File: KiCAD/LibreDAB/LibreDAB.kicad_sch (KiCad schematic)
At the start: 0 parts

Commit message: Added a LV bridge prototype module schematic
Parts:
- added C112: 47uF, Capacitor_SMD:C_Elec_10x10.2, symbol Device:C_Polarized
- added C701: 1nF, Capacitor_SMD:C_0805_2012Metric, symbol Device:C
- added J1, J2, J5: 1x3, 1Footprints:PinHeader_1x03_P2.54mm_Vertical, symbol 1Connectors:PinHeader_1x3_2.54mm
- added J3, J4: Conn_01x02_Socket, symbol Connector:Conn_01x02_Socket
- added LOGO1: N/A, 1Footprints:FFE_Logo_12x12mm_Silk, symbol !Mechanical:FFE_logo
- added Q1, Q2, Q3, Q4: SP010N01BGHTO, 1Footprints:TOLL-8-2_ThermalVias, symbol 1Actives:SP010N01BGHTO
- added R1: 1M, Resistor_SMD:R_0805_2012Metric, symbol Device:R_Small
- added R2: 25.6K, Resistor_SMD:R_0805_2012Metric, symbol Device:R_Small
- added R3: 5mR, Resistor_SMD:R_2512_6332Metric, symbol Device:R_Small
- added TP1, TP2, TP3, TP4, TP5, TP6, TP7, TP8: TestPoint_Probe, Footprints:TestPoint_Pad_D1.0mm, symbol Connector:TestPoint_Probe
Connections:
- new net: J1.2 (Pin_2), J4.2 (Pin_2), Q1.2 (S), Q2.3 (D), TP6.1
- new net: J1.1 (Pin_1), Q1.1 (G), TP7.1
- new net: J1.3 (Pin_3), Q2.1 (G), TP8.1
- new net: C112.1, J3.1 (Pin_1), Q1.3 (D), Q3.3 (D), R1.1, TP2.1
- new net: C701.1, J5.1 (Pin_1), R1.2, R2.1, TP3.1
- new net: C112.2, C701.2, J3.2 (Pin_2), J5.2 (Pin_2), R2.2, R3.2, TP1.1
- new net: J5.3 (Pin_3), Q2.2 (S), Q4.2 (S), R3.1, TP4.1
- new net: J2.3 (Pin_3), Q4.1 (G)
- new net: J2.2 (Pin_2), J4.1 (Pin_1), Q3.2 (S), Q4.3 (D), TP5.1
- new net: J2.1 (Pin_1), Q3.1 (G)
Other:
- note added: "Gate driver pins"
- note added: "Screw Terminals"
- note added: "Voltage and Current sense passives"

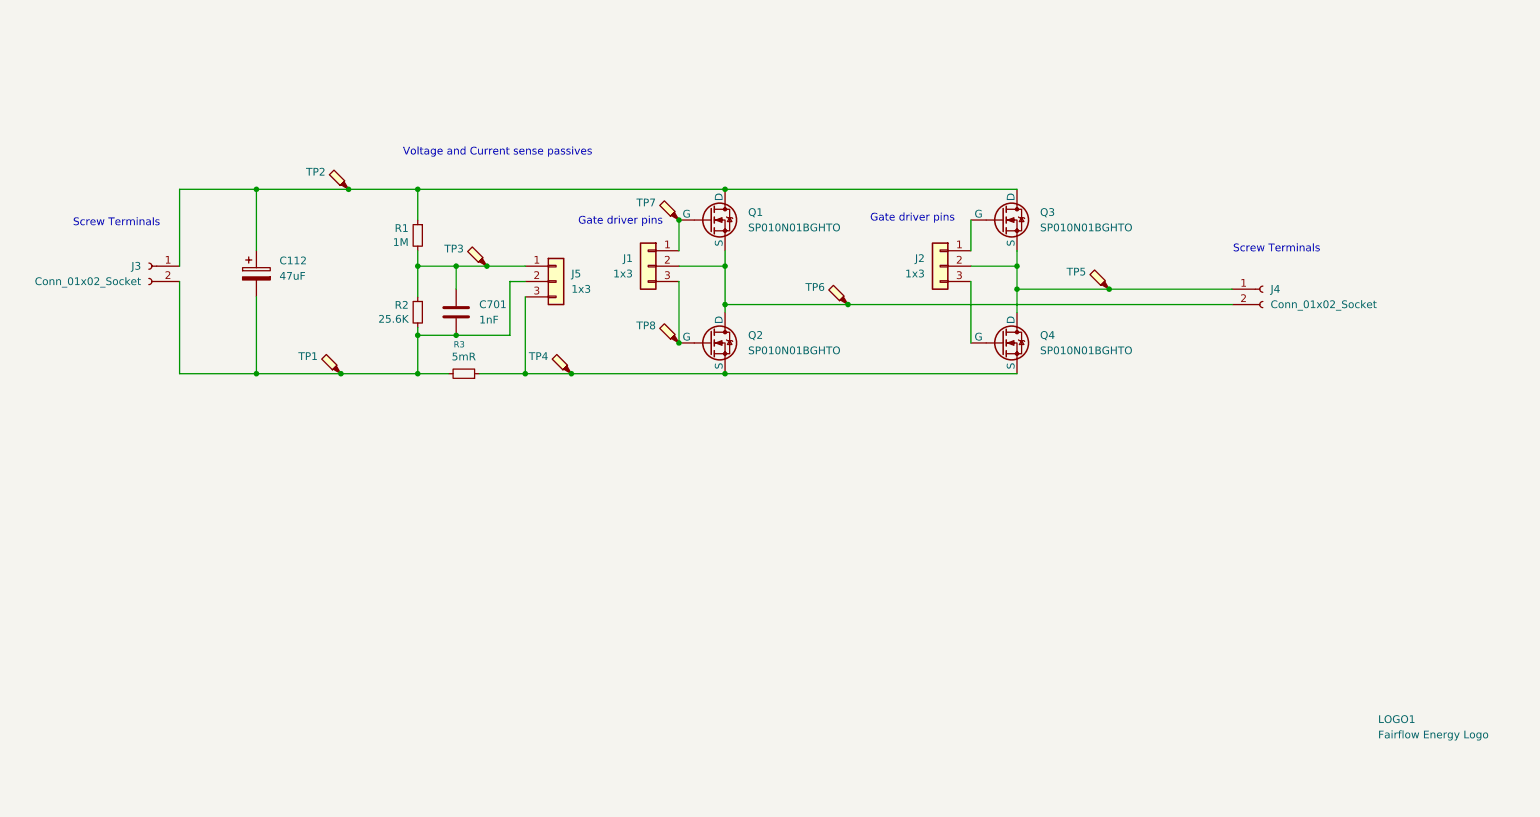
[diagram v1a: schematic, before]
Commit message: Added most footprints from LCSC import
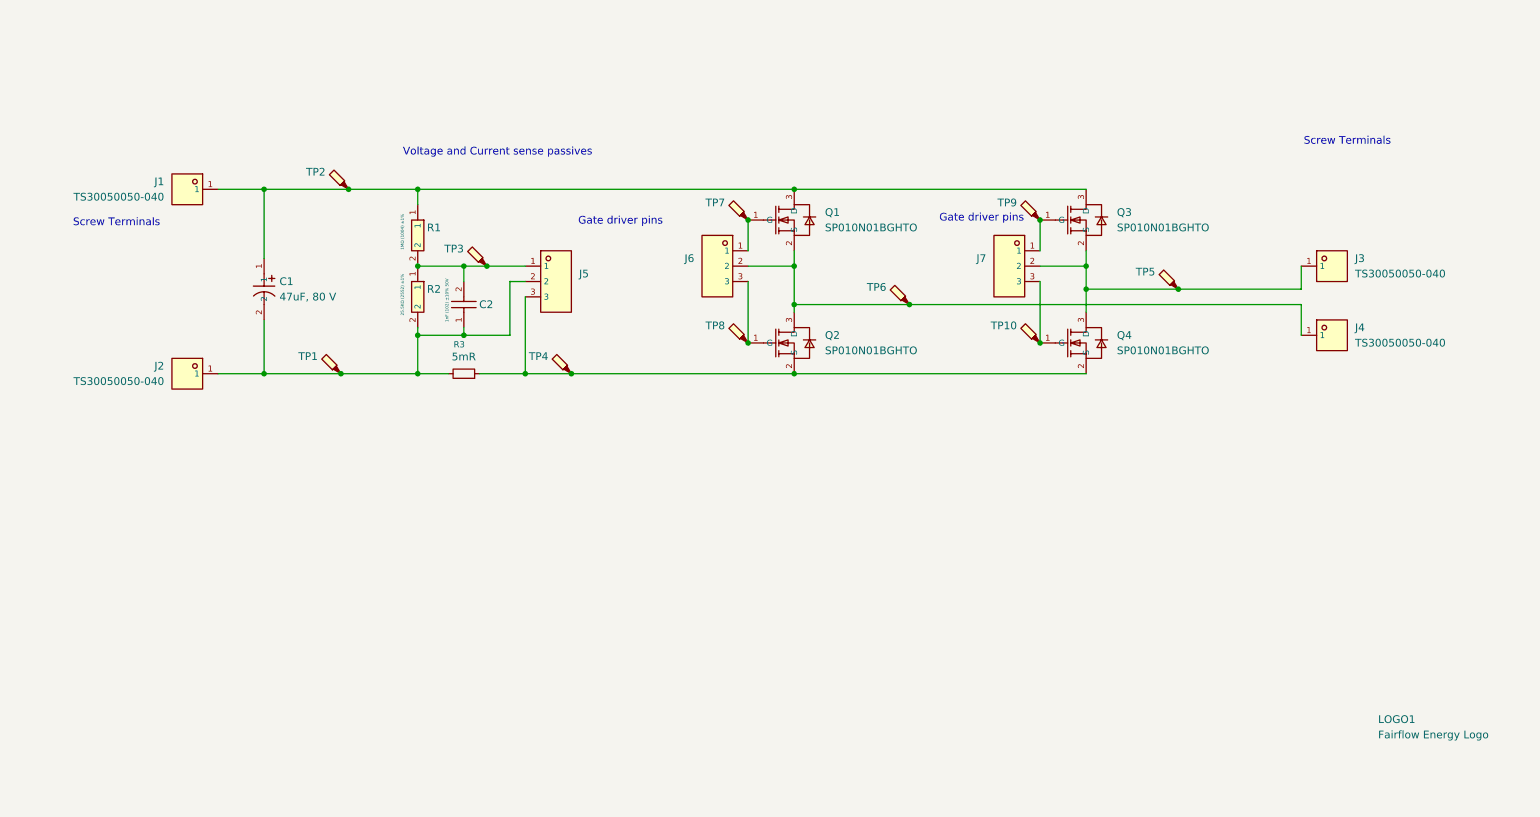
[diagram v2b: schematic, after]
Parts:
- removed C112: 47uF, Capacitor_SMD:C_Elec_10x10.2, symbol Device:C_Polarized
- removed C701: 1nF, Capacitor_SMD:C_0805_2012Metric, symbol Device:C
- removed J1, J2, J5: 1x3, 1Footprints:PinHeader_1x03_P2.54mm_Vertical, symbol 1Connectors:PinHeader_1x3_2.54mm
- removed J3, J4: Conn_01x02_Socket, symbol Connector:Conn_01x02_Socket
- removed Q1, Q2, Q3, Q4: SP010N01BGHTO, 1Footprints:TOLL-8-2_ThermalVias, symbol 1Actives:SP010N01BGHTO
- removed R1: 1M, Resistor_SMD:R_0805_2012Metric, symbol Device:R_Small
- removed R2: 25.6K, Resistor_SMD:R_0805_2012Metric, symbol Device:R_Small
- added C1: 47uF, 80 V, lcsc_footprints:C3031594_CAP-SMD_BD10_0-L10_3-W10_3-FD, symbol lcsc_imported:HBV470M1KTR-1010
- added C2: 1nF (102) ±10% 50V, lcsc_footprints:C46653_C0805, symbol lcsc_imported:1nF_(102)_±10%_50V
- added J1, J2, J3, J4: TS30050050-040, lcsc_footprints:C51018168_SMD_L5_0-W5_0_CON1_5X5_SMD, symbol lcsc_imported:TS30050050-040
- added J5, J6, J7: PZ254VS-11-03P-B01, lcsc_footprints:C41432921_HDR-SMD_3P-P2_54-V-M-LS4_8_R2, symbol lcsc_imported:PZ254VS-11-03P-B01
- added Q1, Q2, Q3, Q4: SP010N01BGHTO, lcsc_footprints:C22385350_TOLL-8_L10_4-W9_9-P1_20-LS11_7-BL_2, symbol lcsc_imported:SP010N01BGHTO
- added R1: 1MΩ (1004) ±1%, lcsc_footprints:C17514_R0805, symbol lcsc_imported:1MΩ_(1004)_±1%
- added R2: 25.5KΩ (2552) ±1%, lcsc_footprints:C46670_R0805, symbol lcsc_imported:25_5KΩ_(2552)_±1%
- added TP10, TP9: TestPoint_Probe, 1Footprints:TestPoint_Pad_D1.0mm, symbol Connector:TestPoint_Probe
- TP1, TP2, TP4, TP5, TP6, TP7, TP8: footprint Footprints:TestPoint_Pad_D1.0mm -> 1Footprints:TestPoint_Pad_D1.0mm
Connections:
- net at TP6.1: now also J4.1, J6.2, Q1.2 (S), Q2.3 (D)
- net at TP7.1: now also J6.1, Q1.1 (G)
- net at TP8.1: now also J6.3, Q2.1 (G)
- net at TP2.1: now also C1.1, J1.1, Q1.3 (D), Q3.3 (D), R1.1
- net at TP3.1: now also C2.2, J5.1, R1.2, R2.1
- net at R3.2, TP1.1: now also C1.2, C2.1, J2.1, J5.2, R2.2
- net at R3.1, TP4.1: now also J5.3, Q2.2 (S), Q4.2 (S)
- net at TP5.1: now also J3.1, J7.2, Q3.2 (S), Q4.3 (D)
- new net: J7.1, Q3.1 (G), TP9.1
- new net: J7.3, Q4.1 (G), TP10.1

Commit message: PCB component placement continues
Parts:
- removed R3: 5mR, Resistor_SMD:R_2512_6332Metric, symbol Device:R_Small
- added H1, H2, H3, H4: M3x3.5, 1Footprints:MountingHole_Pad_SMD_BD5.6-D4.1, symbol Mechanical:MountingHole_Pad
- added R3, R4, R5, R6, R7: 5mΩ ±1% 3W 2512, lcsc_footprints:C393074_RES-SMD_L6_4-W3_2-1, symbol lcsc_imported:RLP25FEGMR005
- TP3: footprint Footprints:TestPoint_Pad_D1.0mm -> 1Footprints:TestPoint_Pad_D1.0mm
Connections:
- net at C1.2, C2.1, J2.1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: now also R3.1, R4.1, R5.1, R6.1, R7.1
- net at J5.3, Q2.2 (S), Q4.2 (S)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: now also R3.2, R4.2, R5.2, R6.2, R7.2
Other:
- note added: "At 80 V maximum voltage, aim for voltage divider to produce 2 V. 2 / 80 = 0.025 ratio Fixing top resistor at 1 MOhm Bottom resistor = 0.025 x 1 Mohm = 25 k 25.5 k is closest value. This will cap the range slightly below 80 V. 1 nF capacitor for minimal low pass filtering."
- note added: "Ipeak = 60 A, bidirectional in short circuit condition Aiming for ~ 72 mV at full range based on uVerter design R = V/I = 72m/60 = 1.2 mOhm Aim for 1 mOhm resistor Check losses: I^2 R = 60^2 * 1m = 3.6 Watts At nominal 35 A: 35^2*1m = 1.225 Watts For thermal capacity, use 5 x 5 mOhm in parallel. Total power rating 5 x 3 W = 15 W."
- note added: "Stored energy: 0.5 CV^2 0.5 * 45u * 80^2 = 0.144 J Discharge time constant: RC ~ 1M * 47u = 45 seconds"

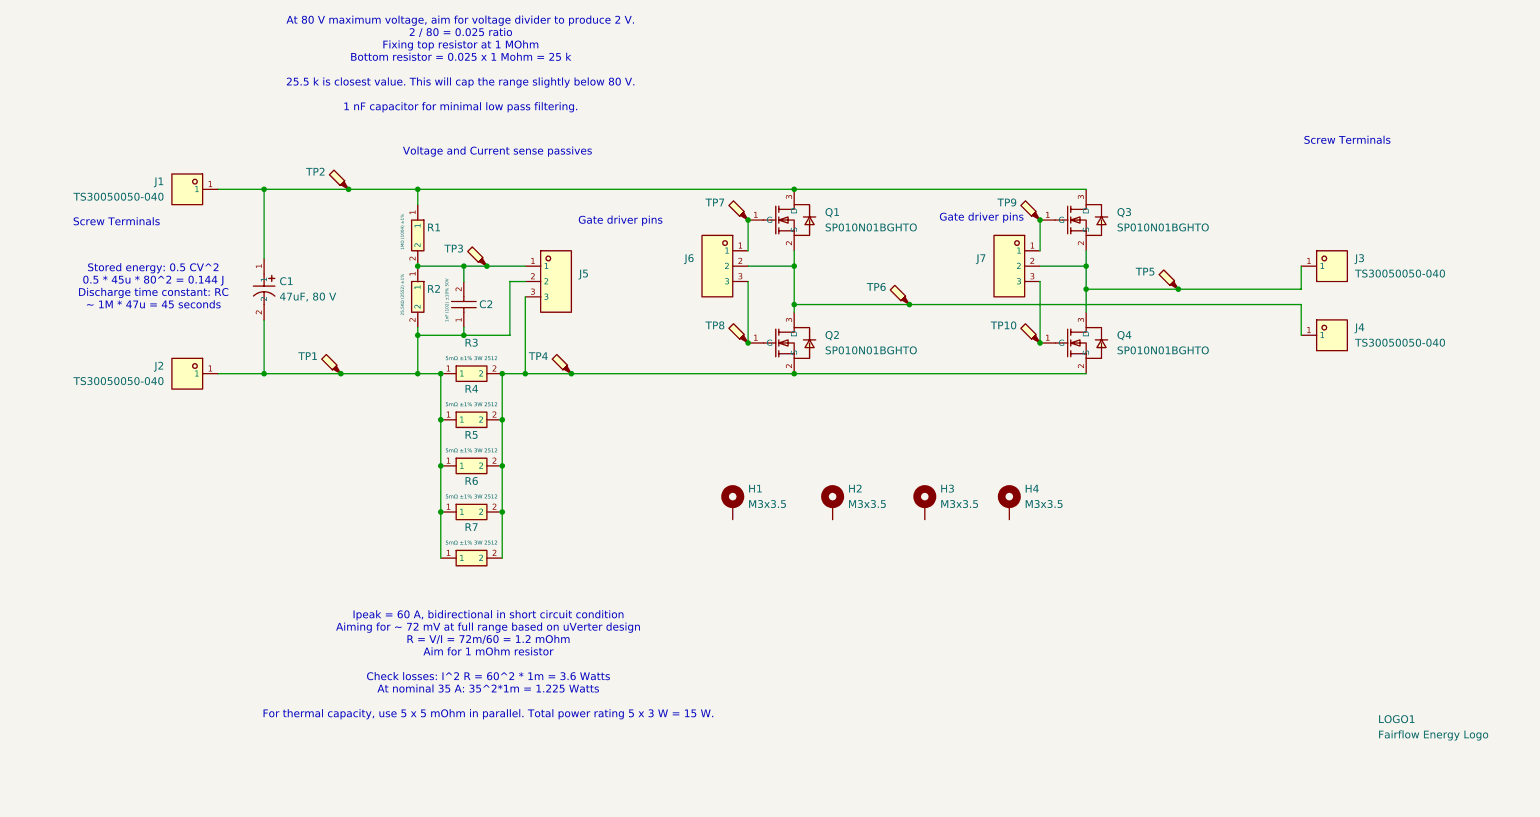
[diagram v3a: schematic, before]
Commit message: Added WIP Gate Driver
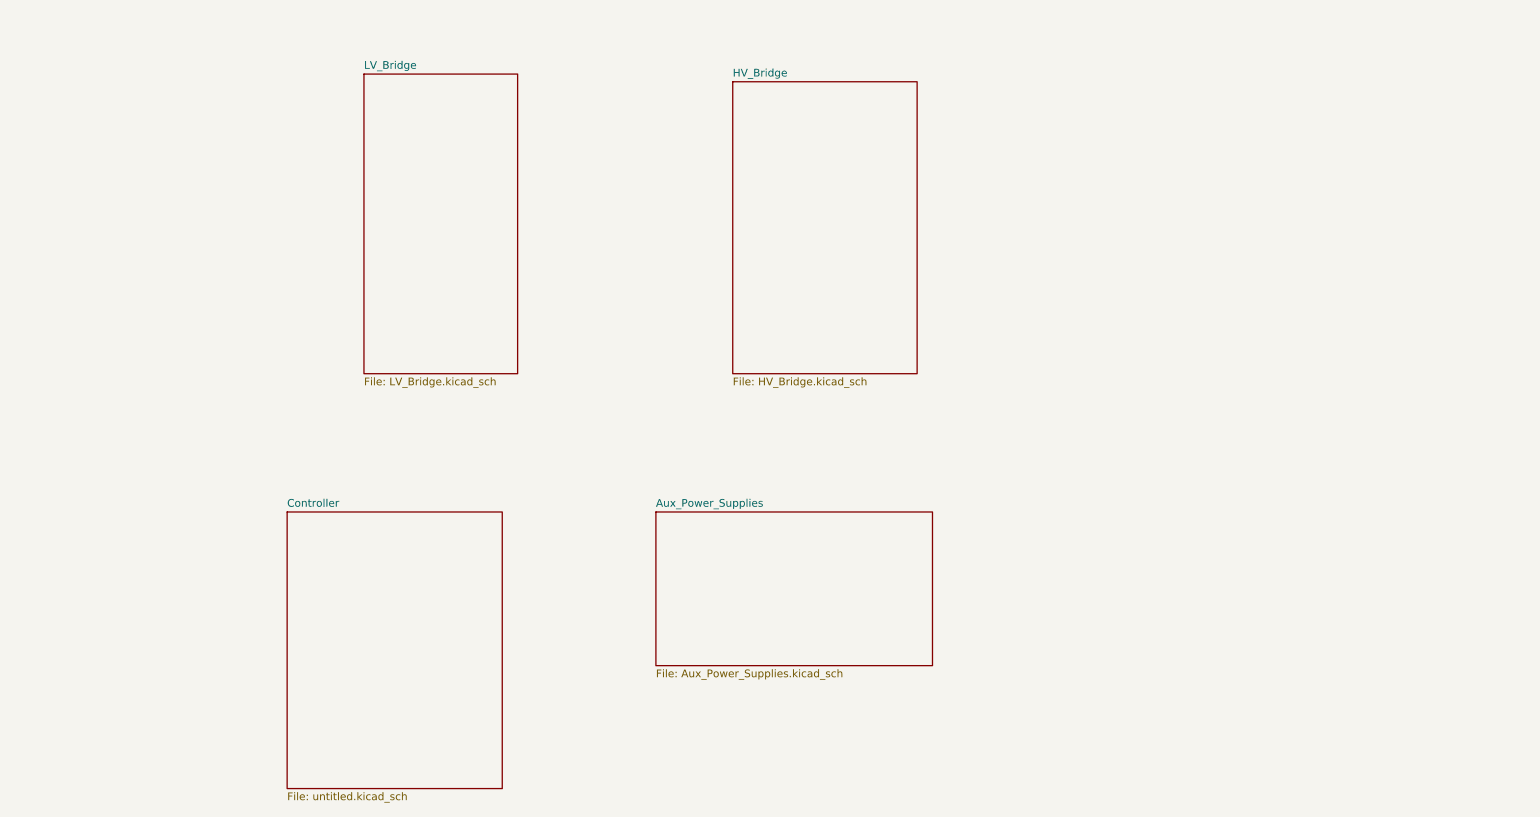
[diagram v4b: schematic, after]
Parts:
- removed C1: 47uF, 80 V, lcsc_footprints:C3031594_CAP-SMD_BD10_0-L10_3-W10_3-FD, symbol lcsc_imported:HBV470M1KTR-1010
- removed C2: 1nF (102) ±10% 50V, lcsc_footprints:C46653_C0805, symbol lcsc_imported:1nF_(102)_±10%_50V
- removed H1, H2, H3, H4: M3x3.5, 1Footprints:MountingHole_Pad_SMD_BD5.6-D4.1, symbol Mechanical:MountingHole_Pad
- removed J1, J2, J3, J4: TS30050050-040, lcsc_footprints:C51018168_SMD_L5_0-W5_0_CON1_5X5_SMD, symbol lcsc_imported:TS30050050-040
- removed J5, J6, J7: PZ254VS-11-03P-B01, lcsc_footprints:C41432921_HDR-SMD_3P-P2_54-V-M-LS4_8_R2, symbol lcsc_imported:PZ254VS-11-03P-B01
- removed LOGO1: N/A, 1Footprints:FFE_Logo_12x12mm_Silk, symbol !Mechanical:FFE_logo
- removed Q1, Q2, Q3, Q4: SP010N01BGHTO, lcsc_footprints:C22385350_TOLL-8_L10_4-W9_9-P1_20-LS11_7-BL_2, symbol lcsc_imported:SP010N01BGHTO
- removed R1: 1MΩ (1004) ±1%, lcsc_footprints:C17514_R0805, symbol lcsc_imported:1MΩ_(1004)_±1%
- removed R2: 25.5KΩ (2552) ±1%, lcsc_footprints:C46670_R0805, symbol lcsc_imported:25_5KΩ_(2552)_±1%
- removed R3, R4, R5, R6, R7: 5mΩ ±1% 3W 2512, lcsc_footprints:C393074_RES-SMD_L6_4-W3_2-1, symbol lcsc_imported:RLP25FEGMR005
- removed TP1, TP10, TP2, TP3, TP4, TP5, TP6, TP7, TP8, TP9: TestPoint_Probe, 1Footprints:TestPoint_Pad_D1.0mm, symbol Connector:TestPoint_Probe
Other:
- added sheet Aux_Power_Supplies (Aux_Power_Supplies.kicad_sch)
- added sheet Controller (untitled.kicad_sch)
- added sheet HV_Bridge (HV_Bridge.kicad_sch)
- added sheet LV_Bridge (LV_Bridge.kicad_sch)
- note removed: "At 80 V maximum voltage, aim for voltage divider to produce 2 V. 2 / 80 = 0.025 ratio Fixing top resistor at 1 MOhm Bottom resistor = 0.025 x 1 Mohm = 25 k 25.5 k is closest value. This will cap the range slightly below 80 V. 1 nF capacitor for minimal low pass filtering."
- note removed: "Gate driver pins"
- note removed: "Ipeak = 60 A, bidirectional in short circuit condition Aiming for ~ 72 mV at full range based on uVerter design R = V/I = 72m/60 = 1.2 mOhm Aim for 1 mOhm resistor Check losses: I^2 R = 60^2 * 1m = 3.6 Watts At nominal 35 A: 35^2*1m = 1.225 Watts For thermal capacity, use 5 x 5 mOhm in parallel. Total power rating 5 x 3 W = 15 W."
- note removed: "Screw Terminals"
- note removed: "Stored energy: 0.5 CV^2 0.5 * 45u * 80^2 = 0.144 J Discharge time constant: RC ~ 1M * 47u = 45 seconds"
- note removed: "Voltage and Current sense passives"
